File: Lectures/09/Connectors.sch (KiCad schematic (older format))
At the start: 4 parts, among them J1 Serial, J2 Digital Pins, J3 I2C, J4 ICSP

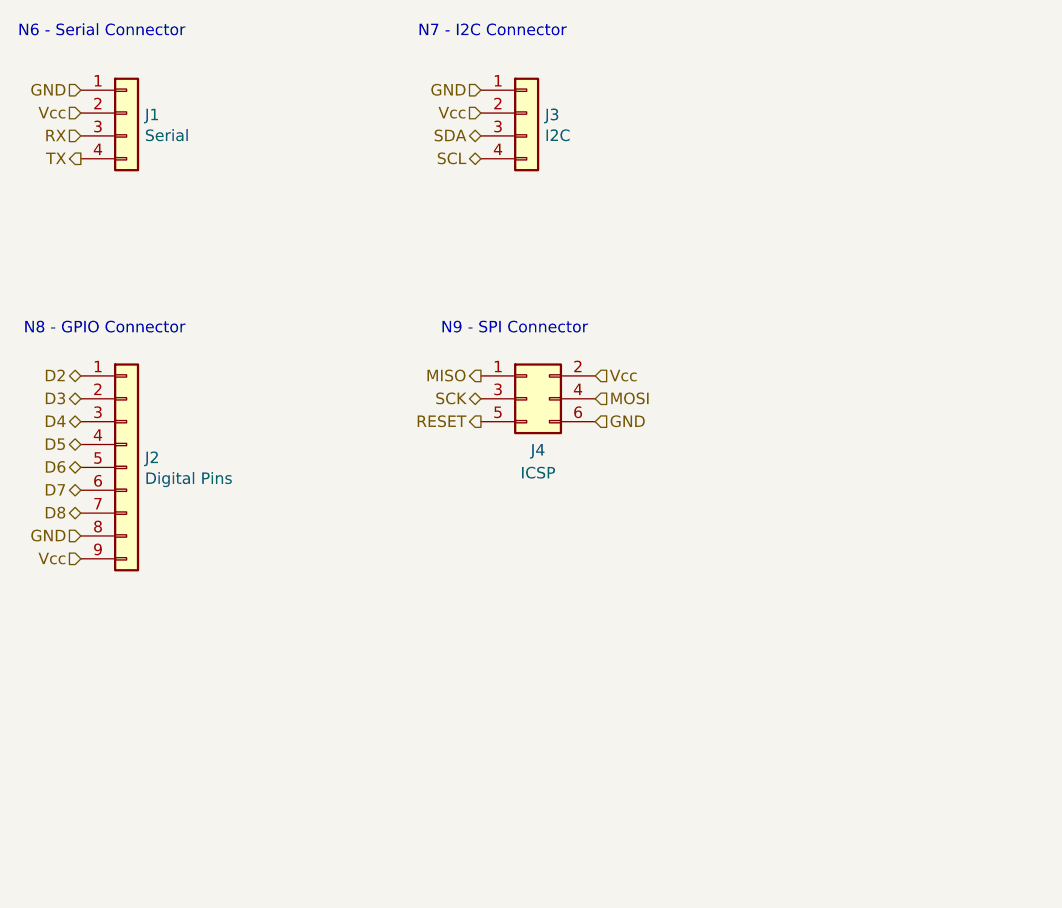
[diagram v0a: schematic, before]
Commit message: Schematic updates
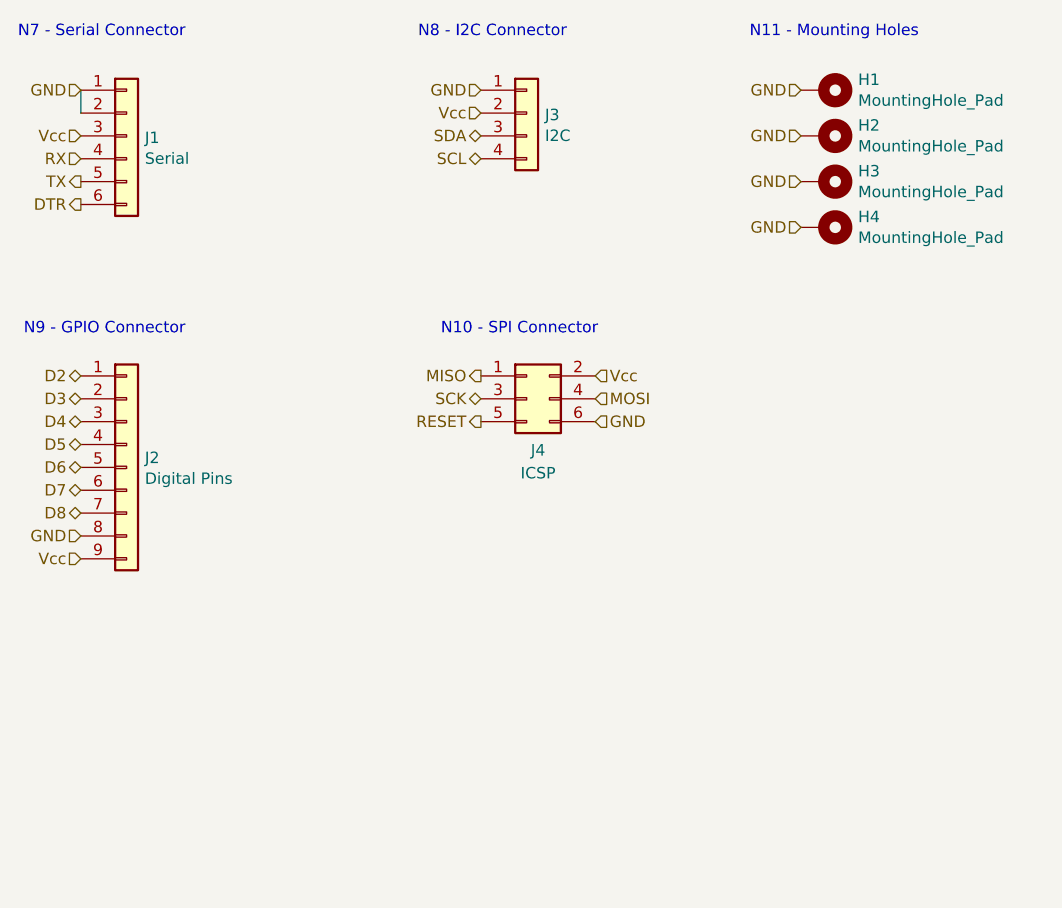
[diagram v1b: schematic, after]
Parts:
- removed J1: Serial, Connector_PinHeader_2.54mm:PinHeader_1x04_P2.54mm_Vertical, symbol Connector_Generic:Conn_01x04
- added H1, H2, H3, H4: MountingHole_Pad, MountingHole:MountingHole_2.2mm_M2_Pad_Via, symbol Mechanical:MountingHole_Pad
- added J1: Serial, Connector_PinHeader_2.54mm:PinHeader_1x06_P2.54mm_Vertical, symbol Connector_Generic:Conn_01x06
- J2: footprint Connector_PinHeader_2.54mm:PinHeader_1x09_P2.54mm_Vertical -> Connector_PinSocket_2.54mm:PinSocket_1x09_P2.54mm_Vertical
- J3: footprint Connector_PinHeader_2.54mm:PinHeader_1x04_P2.54mm_Vertical -> Connector_PinSocket_2.54mm:PinSocket_1x04_P2.54mm_Vertical
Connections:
- net GND: now also H1.1, H2.1, H3.1, H4.1, J1.1 (Pin_1), J1.2 (Pin_2)
- net RX: now also J1.4 (Pin_4)
- net TX: now also J1.5 (Pin_5)
- net Vcc: now also J1.3 (Pin_3)
- new net DTR: J1.6 (Pin_6)
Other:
- note added: "N10 - SPI Connector"
- note added: "N11 - Mounting Holes"
- note added: "N7 - Serial Connector"
- note added: "N8 - I2C Connector"
- note added: "N9 - GPIO Connector"
- note removed: "N6 - Serial Connector"
- note removed: "N7 - I2C Connector"
- note removed: "N8 - GPIO Connector"
- note removed: "N9 - SPI Connector"
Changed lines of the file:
@@
 $EndDescr
-$Comp
-L Connector_Generic:Conn_01x09 J2
-U 1 1 600A0191
-P 4800 4200
-F 0 "J2" H 4880 4242 50  0000 L CNN
-F 1 "Digital Pins" H 4880 4151 50  0000 L CNN
-F 2 "Connector_PinHeader_2.54mm:PinHeader_1x09_P2.54mm_Vertical" H 4800 4200 50  0001 C CNN
-F 3 "~" H 4800 4200 50  0001 C CNN
-	1    4800 4200
-	1    0    0    -1
-$EndComp
 $Comp
 L Connector_Generic:Conn_01x04 J3
@@
 F 0 "J3" H 6630 2642 50  0000 L CNN
 F 1 "I2C" H 6630 2551 50  0000 L CNN
-F 2 "Connector_PinHeader_2.54mm:PinHeader_1x04_P2.54mm_Vertical" H 6550 2650 50  0001 C CNN
+F 2 "Connector_PinSocket_2.54mm:PinSocket_1x04_P2.54mm_Vertical" H 6550 2650 50  0001 C CNN
 F 3 "~" H 6550 2650 50  0001 C CNN
 	1    6550 2650
@@
 F 3 "~" H 6550 3900 50  0001 C CNN
 	1    6550 3900
-	1    0    0    -1
-$EndComp
-$Comp
-L Connector_Generic:Conn_01x04 J1
-U 1 1 600A46E8
-P 4800 2650
-F 0 "J1" H 4880 2642 50  0000 L CNN
-F 1 "Serial" H 4880 2551 50  0000 L CNN
-F 2 "Connector_PinHeader_2.54mm:PinHeader_1x04_P2.54mm_Vertical" H 4800 2650 50  0001 C CNN
-F 3 "~" H 4800 2650 50  0001 C CNN
-	1    4800 2650
 	1    0    0    -1
 $EndComp
@@
 Text HLabel 4600 2550 0    50   Input ~ 0
 GND
-Text HLabel 4600 2650 0    50   Input ~ 0
+Text HLabel 4600 2750 0    50   Input ~ 0
 Vcc
-Text HLabel 4600 2750 0    50   Input ~ 0
+Text HLabel 4600 2850 0    50   Input ~ 0
 RX
-Text HLabel 4600 2850 0    50   Output ~ 0
+Text HLabel 4600 2950 0    50   Output ~ 0
 TX
 Text HLabel 6350 2550 0    50   Input ~ 0
@@
 Vcc
 Text Notes 4325 2325 0    50   ~ 0
-N6 - Serial Connector
+N7 - Serial Connector
 Text Notes 6075 2325 0    50   ~ 0
-N7 - I2C Connector
+N8 - I2C Connector
 Text Notes 4350 3625 0    50   ~ 0
-N8 - GPIO Connector
+N9 - GPIO Connector
 Text Notes 6175 3625 0    50   ~ 0
-N9 - SPI Connector
+N10 - SPI Connector
+Text HLabel 4600 3050 0    50   Output ~ 0
+DTR
+$Comp
+L Connector_Generic:Conn_01x06 J1
+U 1 1 601A66B7
+P 4800 2750
+F 0 "J1" H 4880 2742 50  0000 L CNN
+F 1 "Serial" H 4880 2651 50  0000 L CNN
+F 2 "Connector_PinHeader_2.54mm:PinHeader_1x06_P2.54mm_Vertical" H 4800 2750 50  0001 C CNN
+F 3 "~" H 4800 2750 50  0001 C CNN
+	1    4800 2750
+	1    0    0    -1
+$EndComp
+$Comp
+L Connector_Generic:Conn_01x09 J2
+U 1 1 601AA522
+P 4800 4200
+F 0 "J2" H 4880 4242 50  0000 L CNN
+F 1 "Digital Pins" H 4880 4151 50  0000 L CNN
+F 2 "Connector_PinSocket_2.54mm:PinSocket_1x09_P2.54mm_Vertical" H 4800 4200 50  0001 C CNN
+F 3 "~" H 4800 4200 50  0001 C CNN
+	1    4800 4200
+	1    0    0    -1
+$EndComp
+Wire Wire Line
+	4600 2650 4600 2550
+$Comp
+L Mechanical:MountingHole_Pad H1
+U 1 1 6020F6BA
+P 7850 2550
+F 0 "H1" V 7804 2700 50  0000 L CNN
+F 1 "MountingHole_Pad" V 7895 2700 50  0000 L CNN
+F 2 "MountingHole:MountingHole_2.2mm_M2_Pad_Via" H 7850 2550 50  0001 C CNN
+F 3 "~" H 7850 2550 50  0001 C CNN
+	1    7850 2550
+	0    1    1    0
+$EndComp
+Text HLabel 7750 2550 0    50   Input ~ 0
+GND
+$Comp
+L Mechanical:MountingHole_Pad H2
+U 1 1 602111E4
+P 7850 2750
+F 0 "H2" V 7804 2900 50  0000 L CNN
+F 1 "MountingHole_Pad" V 7895 2900 50  0000 L CNN
+F 2 "MountingHole:MountingHole_2.2mm_M2_Pad_Via" H 7850 2750 50  0001 C CNN
+F 3 "~" H 7850 2750 50  0001 C CNN
+	1    7850 2750
+	0    1    1    0
+$EndComp
+Text HLabel 7750 2750 0    50   Input ~ 0
+GND
+$Comp
+L Mechanical:MountingHole_Pad H3
+U 1 1 6021157E
+P 7850 2950
+F 0 "H3" V 7804 3100 50  0000 L CNN
+F 1 "MountingHole_Pad" V 7895 3100 50  0000 L CNN
+F 2 "MountingHole:MountingHole_2.2mm_M2_Pad_Via" H 7850 2950 50  0001 C CNN
+F 3 "~" H 7850 2950 50  0001 C CNN
+	1    7850 2950
+	0    1    1    0
+$EndComp
+Text HLabel 7750 2950 0    50   Input ~ 0
+GND
+$Comp
+L Mechanical:MountingHole_Pad H4
+U 1 1 60211856
+P 7850 3150
+F 0 "H4" V 7804 3300 50  0000 L CNN
+F 1 "MountingHole_Pad" V 7895 3300 50  0000 L CNN
+F 2 "MountingHole:MountingHole_2.2mm_M2_Pad_Via" H 7850 3150 50  0001 C CNN
+F 3 "~" H 7850 3150 50  0001 C CNN
+	1    7850 3150
+	0    1    1    0
+$EndComp
+Text HLabel 7750 3150 0    50   Input ~ 0
+GND
+Text Notes 7525 2325 0    50   ~ 0
+N11 - Mounting Holes
 $EndSCHEMATC

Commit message: RTC loading capacitors
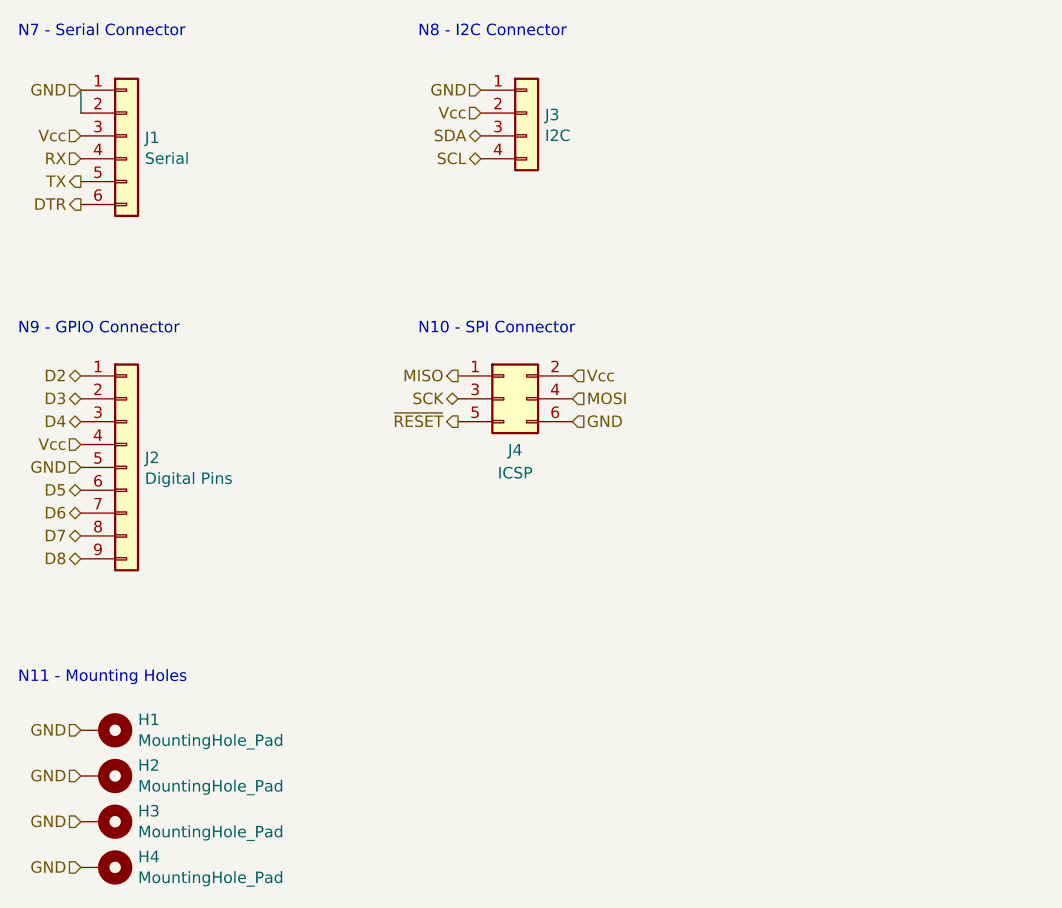
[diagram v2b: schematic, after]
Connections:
- net D5: now also J2.6 (Pin_6); no longer J2.4 (Pin_4)
- net D6: now also J2.7 (Pin_7); no longer J2.5 (Pin_5)
- net D7: now also J2.8 (Pin_8); no longer J2.6 (Pin_6)
- net D8: now also J2.9 (Pin_9); no longer J2.7 (Pin_7)
- net GND: now also J2.5 (Pin_5); no longer J2.8 (Pin_8)
- net Vcc: now also J2.4 (Pin_4); no longer J2.9 (Pin_9)
- net RESET renamed ~RESET
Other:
- moved on the sheet: H1, H2, H3, H4, J4
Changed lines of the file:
@@
 L Connector_Generic:Conn_02x03_Odd_Even J4
 U 1 1 600A23CE
-P 6550 3900
-F 0 "J4" H 6600 3675 50  0000 C CNN
-F 1 "ICSP" H 6600 3575 50  0000 C CNN
-F 2 "Connector_PinHeader_2.54mm:PinHeader_2x03_P2.54mm_Vertical" H 6550 3900 50  0001 C CNN
-F 3 "~" H 6550 3900 50  0001 C CNN
-	1    6550 3900
+P 6450 3900
+F 0 "J4" H 6500 3675 50  0000 C CNN
+F 1 "ICSP" H 6500 3575 50  0000 C CNN
+F 2 "Connector_PinHeader_2.54mm:PinHeader_2x03_P2.54mm_Vertical" H 6450 3900 50  0001 C CNN
+F 3 "~" H 6450 3900 50  0001 C CNN
+	1    6450 3900
 	1    0    0    -1
 $EndComp
-Text HLabel 6350 3800 0    50   Output ~ 0
+Text HLabel 6250 3800 0    50   Output ~ 0
 MISO
-Text HLabel 6350 3900 0    50   BiDi ~ 0
+Text HLabel 6250 3900 0    50   BiDi ~ 0
 SCK
-Text HLabel 6350 4000 0    50   Output ~ 0
-RESET
-Text HLabel 6850 3800 2    50   Input ~ 0
+Text HLabel 6250 4000 0    50   Output ~ 0
+~RESET
+Text HLabel 6750 3800 2    50   Input ~ 0
 Vcc
-Text HLabel 6850 3900 2    50   Input ~ 0
+Text HLabel 6750 3900 2    50   Input ~ 0
 MOSI
-Text HLabel 6850 4000 2    50   Input ~ 0
+Text HLabel 6750 4000 2    50   Input ~ 0
 GND
 Text HLabel 4600 2550 0    50   Input ~ 0
@@
 Text HLabel 4600 4000 0    50   BiDi ~ 0
 D4
-Text HLabel 4600 4100 0    50   BiDi ~ 0
+Text HLabel 4600 4300 0    50   BiDi ~ 0
 D5
-Text HLabel 4600 4200 0    50   BiDi ~ 0
+Text HLabel 4600 4400 0    50   BiDi ~ 0
 D6
-Text HLabel 4600 4300 0    50   BiDi ~ 0
+Text HLabel 4600 4500 0    50   BiDi ~ 0
 D7
-Text HLabel 4600 4400 0    50   BiDi ~ 0
+Text HLabel 4600 4600 0    50   BiDi ~ 0
 D8
-Text HLabel 4600 4500 0    50   Input ~ 0
+Text HLabel 4600 4200 0    50   Input ~ 0
 GND
-Text HLabel 4600 4600 0    50   Input ~ 0
+Text HLabel 4600 4100 0    50   Input ~ 0
 Vcc
 Text Notes 4325 2325 0    50   ~ 0
@@
 Text Notes 6075 2325 0    50   ~ 0
 N8 - I2C Connector
-Text Notes 4350 3625 0    50   ~ 0
+Text Notes 4325 3625 0    50   ~ 0
 N9 - GPIO Connector
-Text Notes 6175 3625 0    50   ~ 0
+Text Notes 6075 3625 0    50   ~ 0
 N10 - SPI Connector
 Text HLabel 4600 3050 0    50   Output ~ 0
@@
 L Mechanical:MountingHole_Pad H1
 U 1 1 6020F6BA
-P 7850 2550
-F 0 "H1" V 7804 2700 50  0000 L CNN
-F 1 "MountingHole_Pad" V 7895 2700 50  0000 L CNN
-F 2 "MountingHole:MountingHole_2.2mm_M2_Pad_Via" H 7850 2550 50  0001 C CNN
-F 3 "~" H 7850 2550 50  0001 C CNN
-	1    7850 2550
+P 4700 5350
+F 0 "H1" V 4654 5500 50  0000 L CNN
+F 1 "MountingHole_Pad" V 4745 5500 50  0000 L CNN
+F 2 "MountingHole:MountingHole_2.2mm_M2_Pad_Via" H 4700 5350 50  0001 C CNN
+F 3 "~" H 4700 5350 50  0001 C CNN
+	1    4700 5350
 	0    1    1    0
 $EndComp
-Text HLabel 7750 2550 0    50   Input ~ 0
+Text HLabel 4600 5350 0    50   Input ~ 0
 GND
 $Comp
 L Mechanical:MountingHole_Pad H2
 U 1 1 602111E4
-P 7850 2750
-F 0 "H2" V 7804 2900 50  0000 L CNN
-F 1 "MountingHole_Pad" V 7895 2900 50  0000 L CNN
-F 2 "MountingHole:MountingHole_2.2mm_M2_Pad_Via" H 7850 2750 50  0001 C CNN
-F 3 "~" H 7850 2750 50  0001 C CNN
-	1    7850 2750
+P 4700 5550
+F 0 "H2" V 4654 5700 50  0000 L CNN
+F 1 "MountingHole_Pad" V 4745 5700 50  0000 L CNN
+F 2 "MountingHole:MountingHole_2.2mm_M2_Pad_Via" H 4700 5550 50  0001 C CNN
+F 3 "~" H 4700 5550 50  0001 C CNN
+	1    4700 5550
 	0    1    1    0
 $EndComp
-Text HLabel 7750 2750 0    50   Input ~ 0
+Text HLabel 4600 5550 0    50   Input ~ 0
 GND
 $Comp
 L Mechanical:MountingHole_Pad H3
 U 1 1 6021157E
-P 7850 2950
-F 0 "H3" V 7804 3100 50  0000 L CNN
-F 1 "MountingHole_Pad" V 7895 3100 50  0000 L CNN
-F 2 "MountingHole:MountingHole_2.2mm_M2_Pad_Via" H 7850 2950 50  0001 C CNN
-F 3 "~" H 7850 2950 50  0001 C CNN
-	1    7850 2950
+P 4700 5750
+F 0 "H3" V 4654 5900 50  0000 L CNN
+F 1 "MountingHole_Pad" V 4745 5900 50  0000 L CNN
+F 2 "MountingHole:MountingHole_2.2mm_M2_Pad_Via" H 4700 5750 50  0001 C CNN
+F 3 "~" H 4700 5750 50  0001 C CNN
+	1    4700 5750
 	0    1    1    0
 $EndComp
-Text HLabel 7750 2950 0    50   Input ~ 0
+Text HLabel 4600 5750 0    50   Input ~ 0
 GND
 $Comp
 L Mechanical:MountingHole_Pad H4
 U 1 1 60211856
-P 7850 3150
-F 0 "H4" V 7804 3300 50  0000 L CNN
-F 1 "MountingHole_Pad" V 7895 3300 50  0000 L CNN
-F 2 "MountingHole:MountingHole_2.2mm_M2_Pad_Via" H 7850 3150 50  0001 C CNN
-F 3 "~" H 7850 3150 50  0001 C CNN
-	1    7850 3150
+P 4700 5950
+F 0 "H4" V 4654 6100 50  0000 L CNN
+F 1 "MountingHole_Pad" V 4745 6100 50  0000 L CNN
+F 2 "MountingHole:MountingHole_2.2mm_M2_Pad_Via" H 4700 5950 50  0001 C CNN
+F 3 "~" H 4700 5950 50  0001 C CNN
+	1    4700 5950
 	0    1    1    0
 $EndComp
-Text HLabel 7750 3150 0    50   Input ~ 0
+Text HLabel 4600 5950 0    50   Input ~ 0
 GND
-Text Notes 7525 2325 0    50   ~ 0
+Text Notes 4325 5150 0    50   ~ 0
 N11 - Mounting Holes
 $EndSCHEMATC
